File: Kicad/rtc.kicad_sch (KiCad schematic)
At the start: 4 parts, among them U801 DS1307Z+, Y801 32,768 Hz

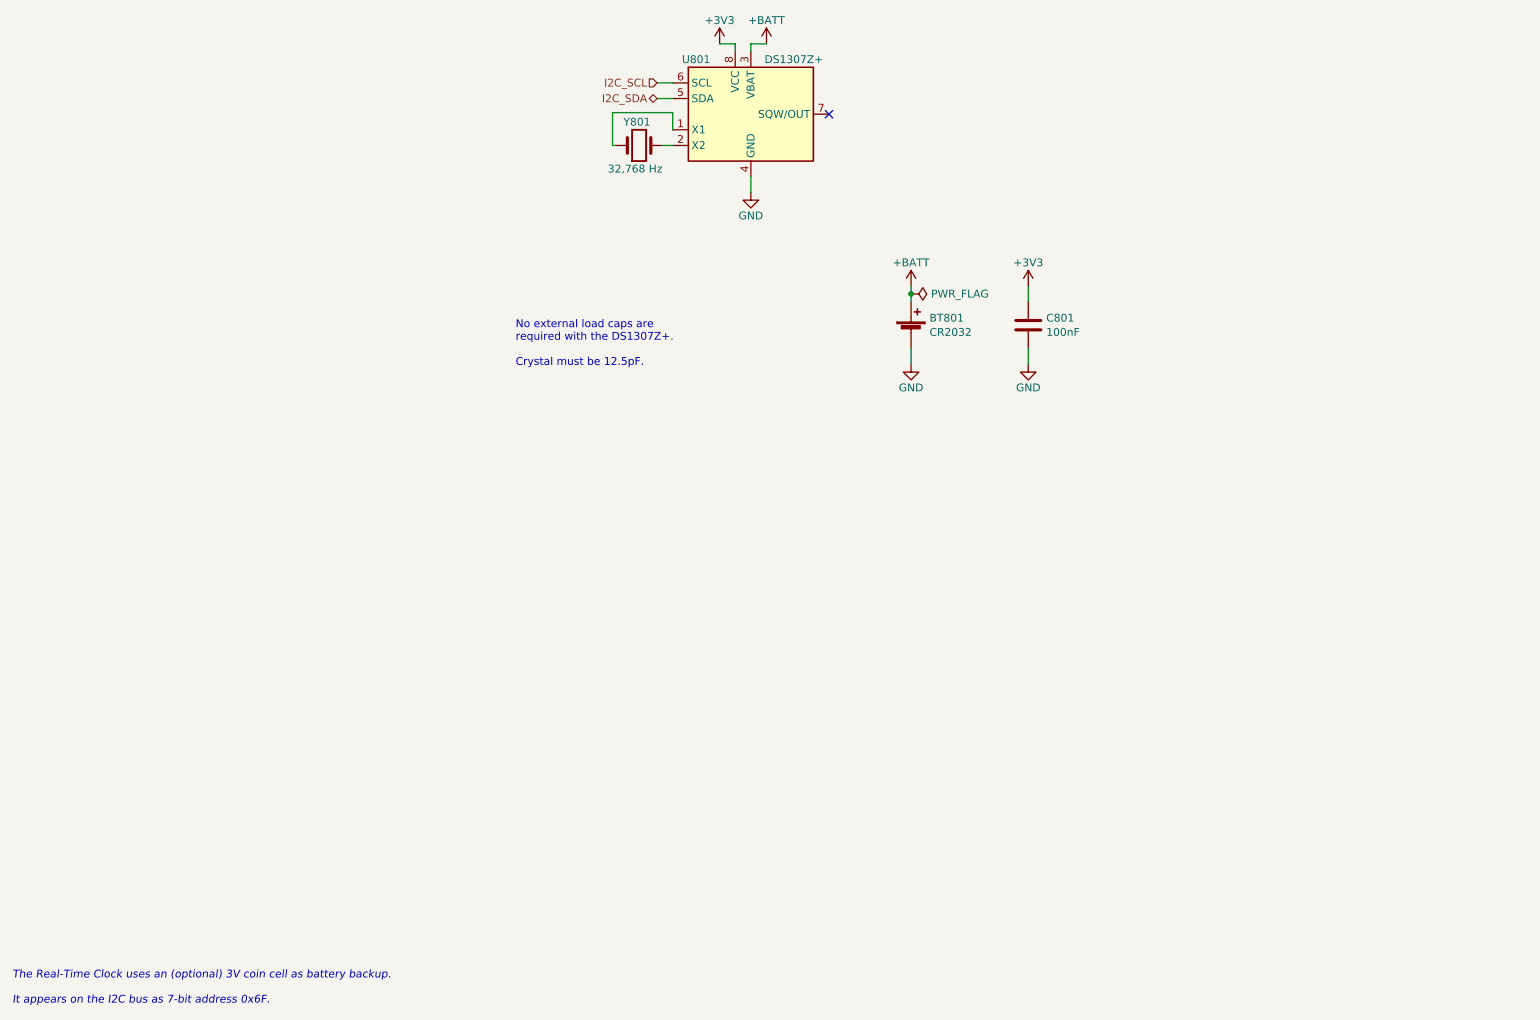
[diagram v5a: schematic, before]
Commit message: Re-organised top sheet.
Lots of parts just changed their component designator. I had
to patch up the PCB manually, but now it imports from the schematic
OK.

Also adds two PSU rails for the RTC (so you can pick DS1307
which is a 5V part, or MCP7940N which is a 3.3V part).
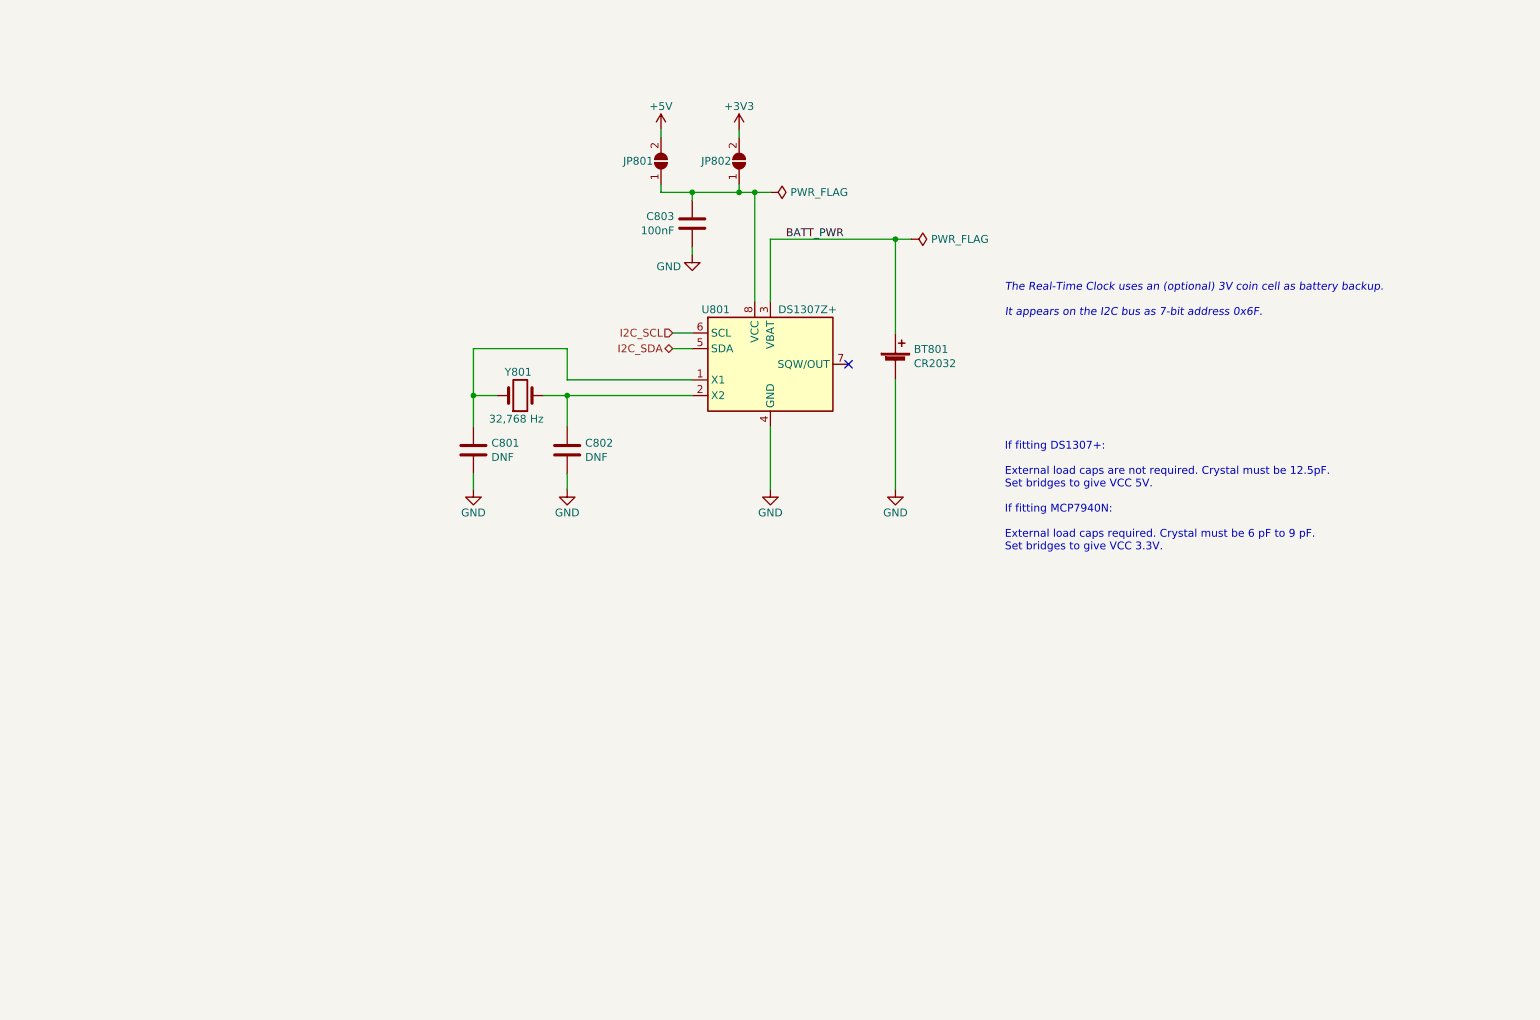
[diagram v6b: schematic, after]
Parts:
- added C801, C802: DNF, Capacitor_SMD:C_0805_2012Metric_Pad1.18x1.45mm_HandSolder, symbol Device:C
- added JP801, JP802: SolderJumper_2_Open, Jumper:SolderJumper-2_P1.3mm_Open_Pad1.0x1.5mm, symbol Jumper:SolderJumper_2_Open
- renumbered C801 to C803
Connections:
- net +3V3: now also JP802.2 (B); no longer C803.1, U801.8 (VCC)
- net GND: now also C801.2, C802.2
- net at U801.1 (X1), Y801.1: now also C801.1
- net at U801.2 (X2), Y801.2: now also C802.1
- net +BATT renamed BATT_PWR
- new net: C803.1, JP801.1 (A), JP802.1 (A), U801.8 (VCC)
- new net +5V: JP801.2 (B)
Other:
- note added: "If fitting DS1307+: External load caps are not required. Crystal must be 12.5pF. Set bridges to give VCC 5V. If fitting MCP7940N: External load caps required. Crystal must be 6 pF to 9 pF. Set bridges to give VCC 3.3V."
- note removed: "No external load caps are required with the DS1307Z+. Crystal must be 12.5pF."
- moved on the sheet: BT801, C803, U801, Y801

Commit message: Cleaned up the part numbers.
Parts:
- C803: Digikey 399-C0805C104M5RAC7800CT-ND -> (none); JLCPCB Collection (none) -> Basic; MPN C0805C104M5RACTU -> CC0805KRX7R9BB104; Manufacturer Kemet -> Yageo; Mouser 80-C0805C104M5R -> (none); Tolerance X5R -> X7R; Voltage 10V -> 50V
- JP801, JP802: value SolderJumper_2_Open -> Bridge
- U801: Digikey DS1307Z+-ND -> (none); JLCPCB Collection (none) -> Extended; Mouser 700-DS1307Z -> (none)
- Y801: Digikey SER4103TR-ND -> (none); JLCPCB Collection (none) -> Basic; MPN FC-135 32.7680KA-A5 -> Q13FC1350000400
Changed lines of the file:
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@@
       (effects (font (size 1.27 1.27)) hide)
     )
-    (property "Manufacturer" "Kemet" (id 4) (at 303.53 153.67 0)
+    (property "Manufacturer" "Yageo" (id 4) (at 303.53 153.67 0)
       (effects (font (size 1.27 1.27)) hide)
     )
@@
       (effects (font (size 1.27 1.27)) hide)
     )
-    (property "Digikey" "399-C0805C104M5RAC7800CT-ND" (id 6) (at 124.46 68.58 0)
-      (effects (font (size 1.27 1.27)) hide)
-    )
-    (property "MPN" "C0805C104M5RACTU" (id 7) (at 124.46 68.58 0)
-      (effects (font (size 1.27 1.27)) hide)
-    )
-    (property "Mouser" "80-C0805C104M5R" (id 8) (at 124.46 68.58 0)
+    (property "Digikey" "~" (id 6) (at 124.46 68.58 0)
+      (effects (font (size 1.27 1.27)) hide)
+    )
+    (property "MPN" "CC0805KRX7R9BB104" (id 7) (at 124.46 68.58 0)
+      (effects (font (size 1.27 1.27)) hide)
+    )
+    (property "Mouser" "~" (id 8) (at 124.46 68.58 0)
       (effects (font (size 1.27 1.27)) hide)
     )
@@
       (effects (font (size 1.27 1.27)) hide)
     )
-    (property "Tolerance" "X5R" (id 10) (at 124.46 68.58 0)
-      (effects (font (size 1.27 1.27)) hide)
-    )
-    (property "Voltage" "10V" (id 11) (at 124.46 68.58 0)
+    (property "Tolerance" "X7R" (id 10) (at 124.46 68.58 0)
+      (effects (font (size 1.27 1.27)) hide)
+    )
+    (property "Voltage" "50V" (id 11) (at 124.46 68.58 0)
+      (effects (font (size 1.27 1.27)) hide)
+    )
+    (property "JLCPCB Collection" "Basic" (id 12) (at 124.46 68.58 0)
       (effects (font (size 1.27 1.27)) hide)
     )
@@
       (effects (font (size 1.27 1.27)) hide)
     )
-    (property "MPN" "FC-135 32.7680KA-A5" (id 6) (at 96.52 96.52 0)
-      (effects (font (size 1.27 1.27)) hide)
-    )
-    (property "Digikey" "SER4103TR-ND" (id 7) (at 96.52 96.52 0)
+    (property "MPN" "Q13FC1350000400" (id 6) (at 96.52 96.52 0)
+      (effects (font (size 1.27 1.27)) hide)
+    )
+    (property "Digikey" "~" (id 7) (at 96.52 96.52 0)
       (effects (font (size 1.27 1.27)) hide)
     )
@@
     )
     (property "Voltage" "~" (id 11) (at 96.52 96.52 0)
+      (effects (font (size 1.27 1.27)) hide)
+    )
+    (property "JLCPCB Collection" "Basic" (id 12) (at 96.52 96.52 0)
       (effects (font (size 1.27 1.27)) hide)
     )
@@
       (effects (font (size 1.27 1.27)) hide)
     )
+    (property "JLCPCB Collection" "~" (id 12) (at 157.48 91.44 0)
+      (effects (font (size 1.27 1.27)) hide)
+    )
     (pin "1")
     (pin "2")
@@
     )
     (property "Voltage" "~" (id 11) (at 88.9 105.41 0)
+      (effects (font (size 1.27 1.27)) hide)
+    )
+    (property "JLCPCB Collection" "~" (id 12) (at 88.9 105.41 0)
       (effects (font (size 1.27 1.27)) hide)
     )
@@
       (effects (font (size 1.27 1.27)) (justify left))
     )
-    (property "Value" "SolderJumper_2_Open" (id 1) (at 128.27 58.42 0)
+    (property "Value" "Bridge" (id 1) (at 128.27 58.42 0)
       (effects (font (size 1.27 1.27)) hide)
     )
@@
       (effects (font (size 1.27 1.27)) hide)
     )
+    (property "JLCPCB Collection" "~" (id 12) (at 132.08 58.42 0)
+      (effects (font (size 1.27 1.27)) hide)
+    )
     (pin "1")
     (pin "2")
@@
       (effects (font (size 1.27 1.27)) (justify left))
     )
-    (property "Value" "SolderJumper_2_Open" (id 1) (at 115.57 58.42 0)
+    (property "Value" "Bridge" (id 1) (at 115.57 58.42 0)
       (effects (font (size 1.27 1.27)) hide)
     )
@@
     )
     (property "Voltage" "~" (id 11) (at 119.38 58.42 0)
+      (effects (font (size 1.27 1.27)) hide)
+    )
+    (property "JLCPCB Collection" "~" (id 12) (at 119.38 58.42 0)
       (effects (font (size 1.27 1.27)) hide)
     )
@@
       (effects (font (size 1.27 1.27)) hide)
     )
+    (property "JLCPCB Collection" "~" (id 12) (at 104.14 105.41 0)
+      (effects (font (size 1.27 1.27)) hide)
+    )
     (pin "1")
     (pin "2")
@@
       (effects (font (size 1.27 1.27)) hide)
     )
-    (property "Datasheet" "https://datasheets.maximintegrated.com/en/ds/DS1307.pdf" (id 3) (at 137.16 91.44 0)
+    (property "Datasheet" "https://datasheet.lcsc.com/lcsc/1809191914_Maxim-Integrated-DS1307Z-T-R_C9868.pdf" (id 3) (at 137.16 91.44 0)
       (effects (font (size 1.27 1.27)) hide)
     )
@@
       (effects (font (size 1.27 1.27)) hide)
     )
-    (property "Digikey" "DS1307Z+-ND" (id 5) (at 137.16 91.44 0)
+    (property "Digikey" "~" (id 5) (at 137.16 91.44 0)
       (effects (font (size 1.27 1.27)) hide)
     )
@@
       (effects (font (size 1.27 1.27)) hide)
     )
-    (property "Mouser" "700-DS1307Z" (id 9) (at 137.16 91.44 0)
+    (property "Mouser" "~" (id 9) (at 137.16 91.44 0)
       (effects (font (size 1.27 1.27)) hide)
     )
@@
       (effects (font (size 1.27 1.27)) hide)
     )
+    (property "JLCPCB Collection" "Extended" (id 12) (at 137.16 91.44 0)
+      (effects (font (size 1.27 1.27)) hide)
+    )

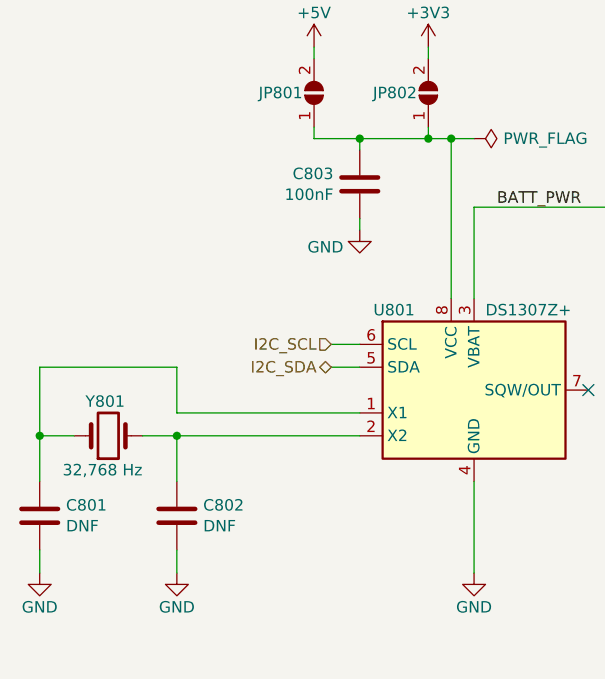
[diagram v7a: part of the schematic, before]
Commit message: Reworked audio circuit.
Based on TLV320AIC23B evaluation board. Removed Pi filters. Used SMD
electrolytic caps for headphone out.
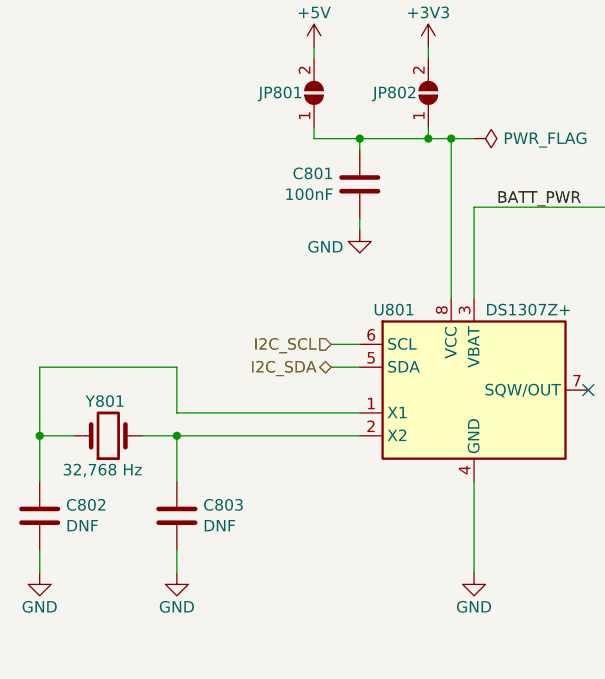
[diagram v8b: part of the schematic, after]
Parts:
- renumbered C803 to C801, C801 to C802, C802 to C803
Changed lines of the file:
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@@
   (symbol (lib_id "Device:C") (at 124.46 68.58 0) (mirror y) (unit 1)
     (in_bom yes) (on_board yes)
-    (property "Reference" "C803" (id 0) (at 121.539 67.4116 0)
+    (property "Reference" "C801" (id 0) (at 121.539 67.4116 0)
       (effects (font (size 1.27 1.27)) (justify left))
     )
@@
   (symbol (lib_id "power:GND") (at 124.46 73.66 0) (unit 1)
     (in_bom yes) (on_board yes)
-    (property "Reference" "#PWR0804" (id 0) (at 124.46 80.01 0)
+    (property "Reference" "#PWR0803" (id 0) (at 124.46 80.01 0)
       (effects (font (size 1.27 1.27)) hide)
     )
@@
   (symbol (lib_id "power:+3V3") (at 132.08 53.34 0) (unit 1)
     (in_bom yes) (on_board yes)
-    (property "Reference" "#PWR0805" (id 0) (at 132.08 57.15 0)
+    (property "Reference" "#PWR0802" (id 0) (at 132.08 57.15 0)
       (effects (font (size 1.27 1.27)) hide)
     )
@@
   (symbol (lib_id "Device:C") (at 88.9 105.41 0) (unit 1)
     (in_bom yes) (on_board yes)
-    (property "Reference" "C801" (id 0) (at 91.821 104.2416 0)
+    (property "Reference" "C802" (id 0) (at 91.821 104.2416 0)
       (effects (font (size 1.27 1.27)) (justify left))
     )
@@
   (symbol (lib_id "power:+5V") (at 119.38 53.34 0) (unit 1)
     (in_bom yes) (on_board yes)
-    (property "Reference" "#PWR0803" (id 0) (at 119.38 57.15 0)
+    (property "Reference" "#PWR0801" (id 0) (at 119.38 57.15 0)
       (effects (font (size 1.27 1.27)) hide)
     )
@@
   (symbol (lib_id "power:GND") (at 104.14 111.76 0) (unit 1)
     (in_bom yes) (on_board yes)
-    (property "Reference" "#PWR0802" (id 0) (at 104.14 118.11 0)
+    (property "Reference" "#PWR0805" (id 0) (at 104.14 118.11 0)
       (effects (font (size 1.27 1.27)) hide)
     )
@@
   (symbol (lib_id "power:GND") (at 88.9 111.76 0) (unit 1)
     (in_bom yes) (on_board yes)
-    (property "Reference" "#PWR0801" (id 0) (at 88.9 118.11 0)
+    (property "Reference" "#PWR0804" (id 0) (at 88.9 118.11 0)
       (effects (font (size 1.27 1.27)) hide)
     )
@@
   (symbol (lib_id "Device:C") (at 104.14 105.41 0) (unit 1)
     (in_bom yes) (on_board yes)
-    (property "Reference" "C802" (id 0) (at 107.061 104.2416 0)
-      (effects (font (size 1.27 1.27)) (justify left))
-    )
+    (property "Reference" "C803" (id 0) (at 107.061 104.2416 0)
+      (effects (font (size 1.27 1.27)) (justify left))
+    )
